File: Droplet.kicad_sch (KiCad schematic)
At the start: 31 parts, among them J1 Conn_01x05, J10 Conn_01x01, J11 Conn_01x01, J12 Conn_01x01, J2 Conn_01x05, J3 Conn_01x01, J4 Conn_01x01, J5 Conn_01x01, J6 Conn_01x01, J7 Conn_01x01, J8 Conn_01x01, J9 Conn_01x01, U1 ATtiny202-SS, U2 IRM-H638T/TR2

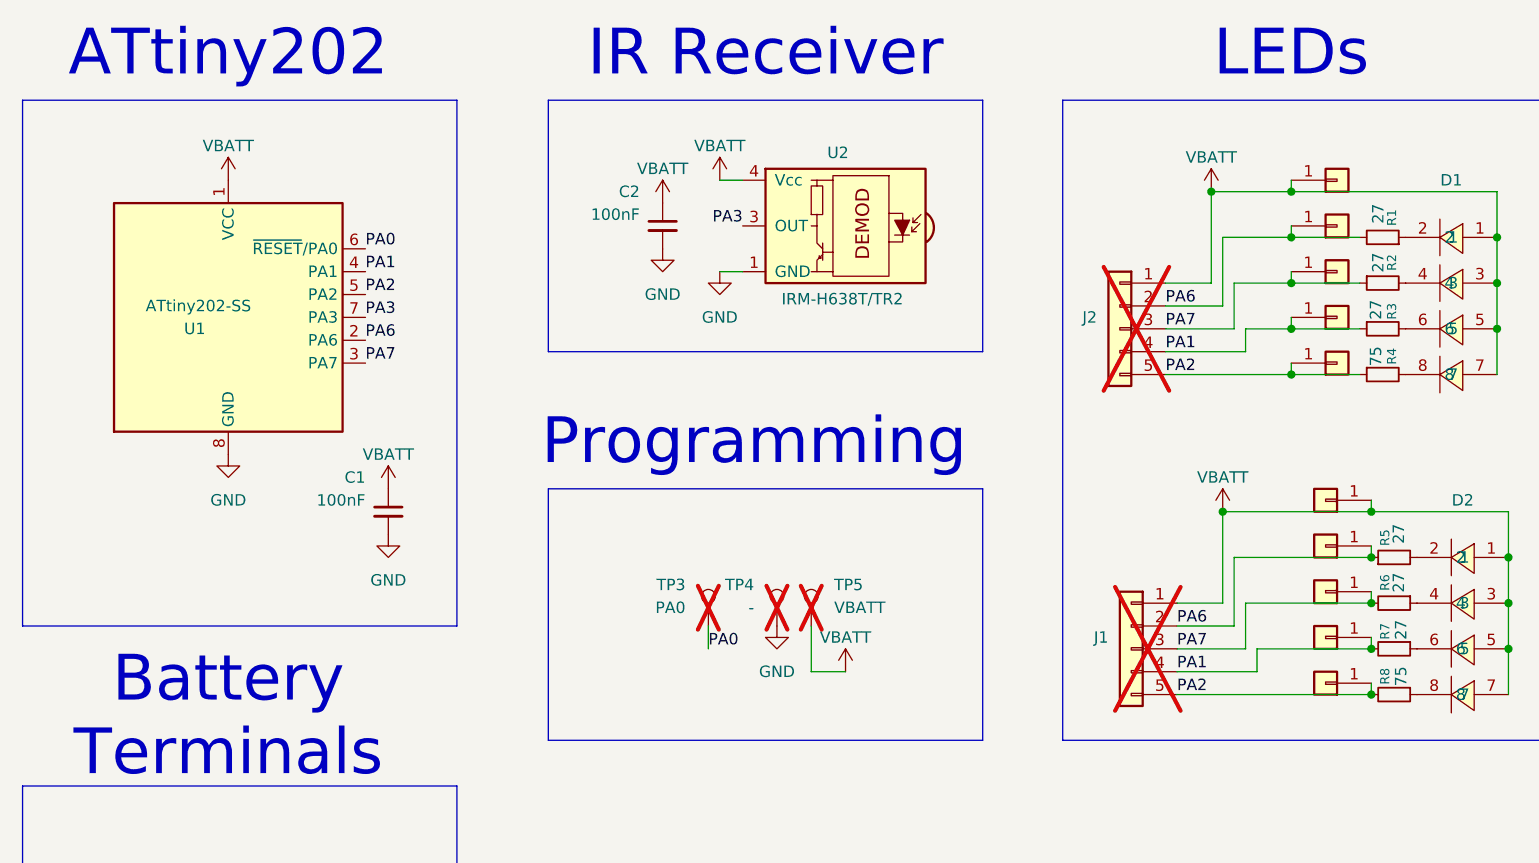
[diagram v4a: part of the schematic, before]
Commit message: 10 LED pair panel
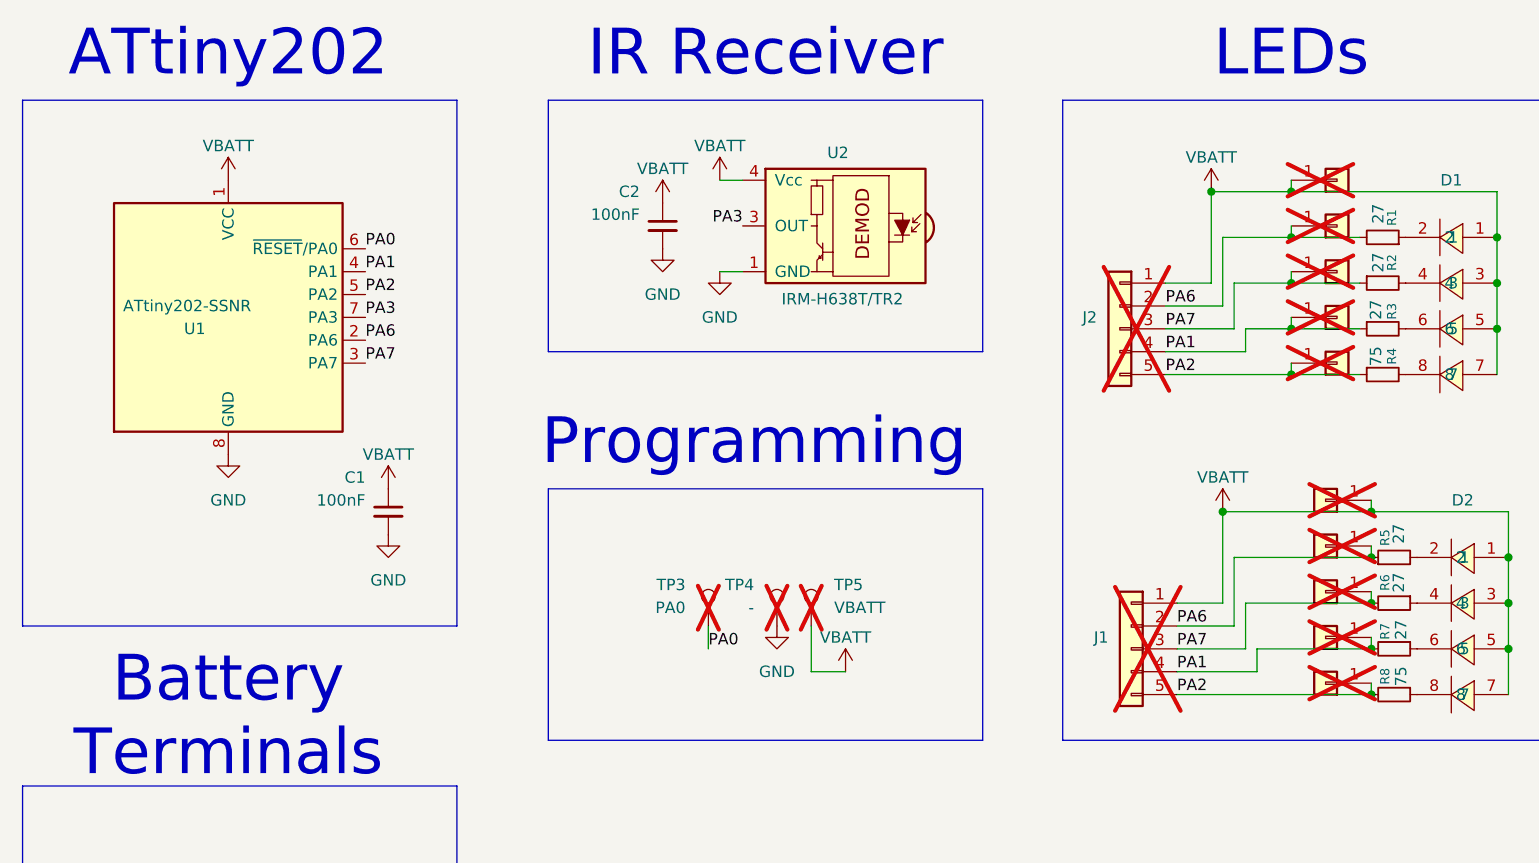
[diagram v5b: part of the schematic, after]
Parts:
- J10, J11, J12, J3, J4, J5, J6, J7, J8, J9: now not fitted; now left out of the parts list
- R1, R2, R3, R5, R6, R7: LCSC Part (none) -> C25100
- R4, R8: LCSC Part (none) -> C25133
- U1: value ATtiny202-SS -> ATtiny202-SSNR
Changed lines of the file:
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@@
 			)
 		)
+		(property "LCSC Part" "C25100"
+			(at 176.53 50.8 0)
+			(effects
+				(font
+					(size 1.27 1.27)
+				)
+				(hide yes)
+			)
+		)
 		(pin "2"
 		)
@@
 			)
 		)
+		(property "LCSC Part" "C25100"
+			(at 177.8 76.2 0)
+			(effects
+				(font
+					(size 1.27 1.27)
+				)
+				(hide yes)
+			)
+		)
 		(pin "2"
 		)
@@
 			)
 		)
+		(property "LCSC Part" "C25133"
+			(at 176.53 55.88 0)
+			(effects
+				(font
+					(size 1.27 1.27)
+				)
+				(hide yes)
+			)
+		)
 		(pin "2"
 		)
@@
 			)
 		)
+		(property "LCSC Part" "C25133"
+			(at 177.8 91.44 0)
+			(effects
+				(font
+					(size 1.27 1.27)
+				)
+				(hide yes)
+			)
+		)
 		(pin "2"
 		)
@@
 		(unit 1)
 		(exclude_from_sim no)
-		(in_bom yes)
+		(in_bom no)
 		(on_board yes)
-		(dnp no)
+		(dnp yes)
 		(fields_autoplaced yes)
 		(property "Reference" "J3"
@@
 			)
 		)
-		(property "Value" "ATtiny202-SS"
+		(property "Value" "ATtiny202-SSNR"
 			(at 50.8 48.26 0)
 			(effects
@@
 		(unit 1)
 		(exclude_from_sim no)
-		(in_bom yes)
+		(in_bom no)
 		(on_board yes)
-		(dnp no)
+		(dnp yes)
 		(fields_autoplaced yes)
 		(property "Reference" "J4"
@@
 			)
 		)
+		(property "LCSC Part" "C25100"
+			(at 176.53 45.72 0)
+			(effects
+				(font
+					(size 1.27 1.27)
+				)
+				(hide yes)
+			)
+		)
 		(pin "2"
 		)
@@
 		(unit 1)
 		(exclude_from_sim no)
-		(in_bom yes)
+		(in_bom no)
 		(on_board yes)
-		(dnp no)
+		(dnp yes)
 		(fields_autoplaced yes)
 		(property "Reference" "J11"
@@
 		(unit 1)
 		(exclude_from_sim no)
-		(in_bom yes)
+		(in_bom no)
 		(on_board yes)
-		(dnp no)
+		(dnp yes)
 		(fields_autoplaced yes)
 		(property "Reference" "J12"
@@
 		(unit 1)
 		(exclude_from_sim no)
-		(in_bom yes)
+		(in_bom no)
 		(on_board yes)
-		(dnp no)
+		(dnp yes)
 		(fields_autoplaced yes)
 		(property "Reference" "J9"
@@
 			)
 		)
+		(property "LCSC Part" "C25100"
+			(at 177.8 86.36 0)
+			(effects
+				(font
+					(size 1.27 1.27)
+				)
+				(hide yes)
+			)
+		)
 		(pin "2"
 		)
@@
 		(unit 1)
 		(exclude_from_sim no)
-		(in_bom yes)
+		(in_bom no)
 		(on_board yes)
-		(dnp no)
+		(dnp yes)
 		(fields_autoplaced yes)
 		(property "Reference" "J6"
@@
 		(unit 1)
 		(exclude_from_sim no)
-		(in_bom yes)
+		(in_bom no)
 		(on_board yes)
-		(dnp no)
+		(dnp yes)
 		(fields_autoplaced yes)
 		(property "Reference" "J8"
@@
 		(unit 1)
 		(exclude_from_sim no)
-		(in_bom yes)
+		(in_bom no)
 		(on_board yes)
-		(dnp no)
+		(dnp yes)
 		(fields_autoplaced yes)
 		(property "Reference" "J10"
@@
 			)
 		)
+		(property "LCSC Part" "C25100"
+			(at 177.8 81.28 0)
+			(effects
+				(font
+					(size 1.27 1.27)
+				)
+				(hide yes)
+			)
+		)
 		(pin "2"
 		)
@@
 		(unit 1)
 		(exclude_from_sim no)
-		(in_bom yes)
+		(in_bom no)
 		(on_board yes)
-		(dnp no)
+		(dnp yes)
 		(fields_autoplaced yes)
 		(property "Reference" "J7"
@@
 			)
 		)
+		(property "LCSC Part" "C25100"
+			(at 176.53 40.64 0)
+			(effects
+				(font
+					(size 1.27 1.27)
+				)
+				(hide yes)
+			)
+		)
 		(pin "2"
 		)
@@
 		(unit 1)
 		(exclude_from_sim no)
-		(in_bom yes)
+		(in_bom no)
 		(on_board yes)
-		(dnp no)
+		(dnp yes)
 		(fields_autoplaced yes)
 		(property "Reference" "J5"

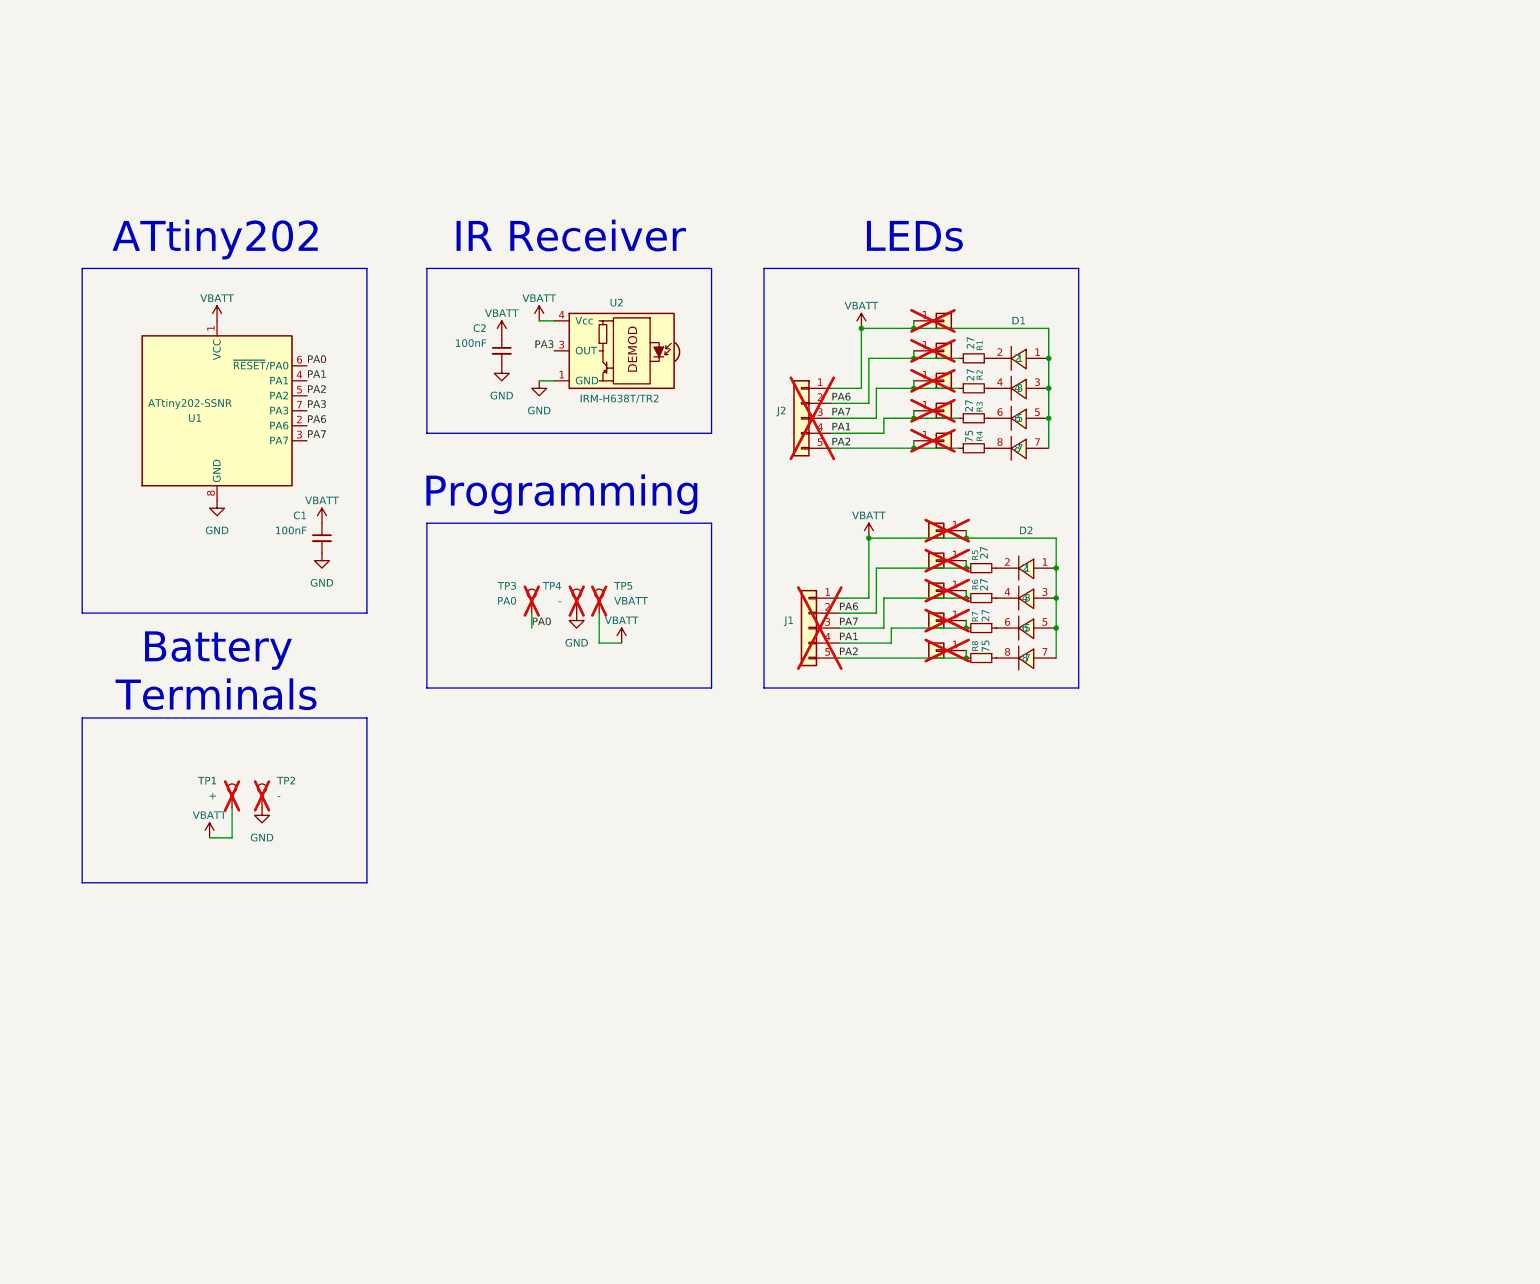
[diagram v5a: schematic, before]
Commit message: major changes - add boost and mosfets
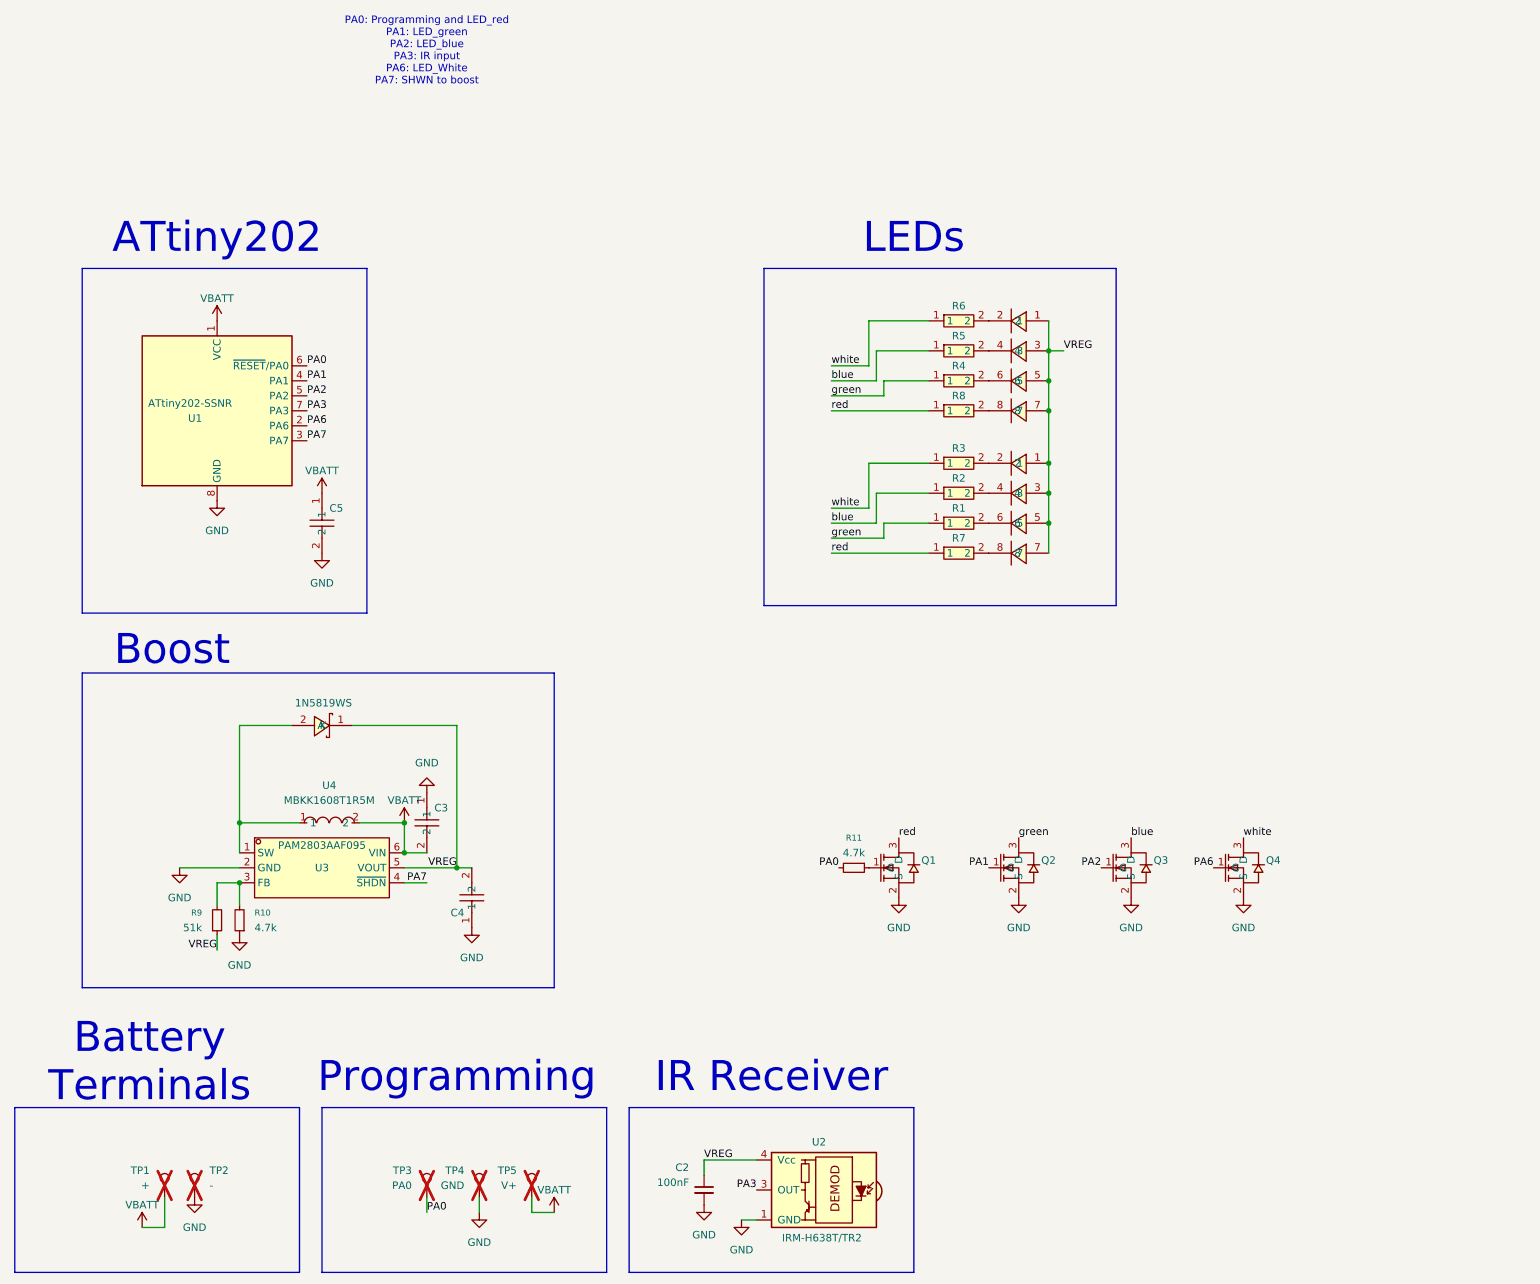
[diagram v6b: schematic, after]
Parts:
- removed C1: 100nF, Capacitor_SMD:C_0402_1005Metric, symbol SparkFun-Capacitor:C_Small
- removed J1, J2: Conn_01x05, Connector_PinHeader_1.00mm:PinHeader_1x05_P1.00mm_Vertical, symbol Connector_Generic:Conn_01x05
- removed J10, J11, J12, J3, J4, J5, J6, J7, J8, J9: Conn_01x01, Custom:1x01_P2.54mm castellated, symbol Connector_Generic:Conn_01x01
- removed R1, R2, R3, R5, R6, R7: 27, Resistor_SMD:R_0402_1005Metric, symbol Device:R_Small
- removed R4, R8: 75, Resistor_SMD:R_0402_1005Metric, symbol Device:R_Small
- added C3, C4, C5: CL05A475MP5NRNC, easyeda2kicad:C0402, symbol easyeda2kicad:CL05A475MP5NRNC
- added D3: 1N5819WS, easyeda2kicad:SOD-323_L1.8-W1.3-LS2.5-RD, symbol easyeda2kicad:1N5819WS
- added Q1, Q2, Q3, Q4: BSS138W_C28646265, easyeda2kicad:SOT-323-3_L2.1-W1.3-P1.30-LS2.3-BR, symbol easyeda2kicad:BSS138W_C28646265
- added R1, R2, R3, R4, R5, R6: 0402WGF1502TCE, easyeda2kicad:R0402, symbol easyeda2kicad:0402WGF1502TCE
- added R10, R11: 4.7k, Resistor_SMD:R_0402_1005Metric, symbol Device:R_Small
- added R7, R8: 0402WGF4702TCE, easyeda2kicad:R0402, symbol easyeda2kicad:0402WGF4702TCE
- added R9: 51k, Resistor_SMD:R_0402_1005Metric, symbol Device:R_Small
- added U3: PAM2803AAF095, easyeda2kicad:SOT-23-6_L2.9-W1.6-P0.95-LS2.8-BR, symbol easyeda2kicad:PAM2803AAF095
- added U4: MBKK1608T1R5M, easyeda2kicad:L0603, symbol easyeda2kicad:MBKK1608T1R5M
- TP4: value - -> GND
- TP5: value VBATT -> V+
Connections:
- net GND: now also C3.1, C4.1, C5.2, Q1.2 (S), Q2.2 (S), Q3.2 (S), Q4.2 (S), R10.1, U3.2 (GND)
- net PA0: now also R11.2
- net PA1: now also Q2.1 (G)
- net PA2: now also Q3.1 (G)
- net PA6: now also Q4.1 (G)
- net PA7: now also U3.4 (~{SHDN})
- net VBATT: now also C3.2, C5.1, U3.6 (VIN), U4.2; no longer C2.1, D1.1, D1.3, D1.5, D1.7, D2.1, D2.3, D2.5, D2.7, U2.4 (Vcc)
- net at D1.6: now also R4.2
- net at D1.2: now also R6.2
- net at D1.4: now also R5.2
- net at D1.8: now also R8.2
- net at D2.2: now also R3.2
- net at D2.8: now also R7.2
- net at D2.6: now also R1.2
- net at D2.4: now also R2.2
- new net: Q1.1 (G), R11.1
- new net: D3.2 (A), U3.1 (SW), U4.1
- new net: R10.2, R9.2, U3.3 (FB)
- new net VREG: C2.1, C4.2, D1.1, D1.3, D1.5, D1.7, D2.1, D2.3, D2.5, D2.7, D3.1 (K), R9.1, U2.4 (Vcc), U3.5 (VOUT)
- new net blue: Q3.3 (D), R2.1, R5.1
- new net green: Q2.3 (D), R1.1, R4.1
- new net red: Q1.3 (D), R7.1, R8.1
- new net white: Q4.3 (D), R3.1, R6.1
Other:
- note added: "Boost"
- note added: "PA0: Programming and LED_red PA1: LED_green PA2: LED_blue PA3: IR input PA6: LED_White PA7: SHWN to boost"
- moved on the sheet: C2, TP1, TP2, TP3, U2
